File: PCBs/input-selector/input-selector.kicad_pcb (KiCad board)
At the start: 2 copper layers, 90.2 x 52.1 mm, 47 parts, among them J1 Conn_01x06_Male, K1 IM40, K2 IM40, K3 IM40, K4 IM40, K5 IM40, K6 IM40, U1 ULN2003, U2 MCP23S17_SO, U3 ULN2003

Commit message: small input selector update
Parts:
- C1: moved to B.Cu
- moved C1 8.39 mm to (127.8, 106.7)
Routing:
- net VDD: track 173.7 -> 172.4 mm
- net GND: vias 0 -> 3
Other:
- net class power: trace_width 0.8 -> 0.381
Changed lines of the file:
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@@
     (thickness 1.6)
     (drawings 25)
-    (tracks 328)
+    (tracks 333)
     (zones 0)
     (modules 47)
@@
   (net_class power ""
     (clearance 0.1524)
-    (trace_width 0.8)
+    (trace_width 0.381)
     (via_dia 0.8)
     (via_drill 0.3302)
@@
     )
   )
-  (module Capacitor_SMD:C_1206_3216Metric_Pad1.42x1.75mm_HandSolder (layer F.Cu)
-    (at 135.255 110.49 270)
+  (module Capacitor_SMD:C_1206_3216Metric_Pad1.42x1.75mm_HandSolder (layer B.Cu)
+    (at 127.762 106.7165 270)
     (descr "Capacitor SMD 1206 (3216 Metric), square (rectangular) end terminal, IPC_7351 nominal with elongated pad for handsoldering. (Body size source: http://www.tortai-tech.com/upload/download/2011102023233369053.pdf), generated with kicad-footprint-generator")
     (tags "capacitor handsolder")
     (attr smd)
-    (fp_text reference C1 (at 0 -1.82 270) (layer F.SilkS)
-      (effects (font (size 1 1) (thickness 0.15)))
+    (fp_text reference C1 (at 0 1.82 270) (layer B.SilkS)
+      (effects (font (size 1 1) (thickness 0.15)) (justify mirror))
     )
-    (fp_text value C (at 0 1.82 270) (layer F.Fab)
-      (effects (font (size 1 1) (thickness 0.15)))
+    (fp_text value C (at 0 -1.82 270) (layer B.Fab)
+      (effects (font (size 1 1) (thickness 0.15)) (justify mirror))
     )
-    (fp_line (start -1.6 0.8) (end -1.6 -0.8) (layer F.Fab) (width 0.1))
-    (fp_line (start -1.6 -0.8) (end 1.6 -0.8) (layer F.Fab) (width 0.1))
-    (fp_line (start 1.6 -0.8) (end 1.6 0.8) (layer F.Fab) (width 0.1))
-    (fp_line (start 1.6 0.8) (end -1.6 0.8) (layer F.Fab) (width 0.1))
-    (fp_line (start -0.602064 -0.91) (end 0.602064 -0.91) (layer F.SilkS) (width 0.12))
-    (fp_line (start -0.602064 0.91) (end 0.602064 0.91) (layer F.SilkS) (width 0.12))
-    (fp_line (start -2.45 1.12) (end -2.45 -1.12) (layer F.CrtYd) (width 0.05))
-    (fp_line (start -2.45 -1.12) (end 2.45 -1.12) (layer F.CrtYd) (width 0.05))
-    (fp_line (start 2.45 -1.12) (end 2.45 1.12) (layer F.CrtYd) (width 0.05))
-    (fp_line (start 2.45 1.12) (end -2.45 1.12) (layer F.CrtYd) (width 0.05))
-    (fp_text user %R (at 0 0 270) (layer F.Fab)
-      (effects (font (size 0.8 0.8) (thickness 0.12)))
+    (fp_line (start -1.6 -0.8) (end -1.6 0.8) (layer B.Fab) (width 0.1))
+    (fp_line (start -1.6 0.8) (end 1.6 0.8) (layer B.Fab) (width 0.1))
+    (fp_line (start 1.6 0.8) (end 1.6 -0.8) (layer B.Fab) (width 0.1))
+    (fp_line (start 1.6 -0.8) (end -1.6 -0.8) (layer B.Fab) (width 0.1))
+    (fp_line (start -0.602064 0.91) (end 0.602064 0.91) (layer B.SilkS) (width 0.12))
+    (fp_line (start -0.602064 -0.91) (end 0.602064 -0.91) (layer B.SilkS) (width 0.12))
+    (fp_line (start -2.45 -1.12) (end -2.45 1.12) (layer B.CrtYd) (width 0.05))
+    (fp_line (start -2.45 1.12) (end 2.45 1.12) (layer B.CrtYd) (width 0.05))
+    (fp_line (start 2.45 1.12) (end 2.45 -1.12) (layer B.CrtYd) (width 0.05))
+    (fp_line (start 2.45 -1.12) (end -2.45 -1.12) (layer B.CrtYd) (width 0.05))
+    (fp_text user %R (at 0 0 270) (layer B.Fab)
+      (effects (font (size 0.8 0.8) (thickness 0.12)) (justify mirror))
     )
-    (pad 1 smd roundrect (at -1.4875 0 270) (size 1.425 1.75) (layers F.Cu F.Paste F.Mask) (roundrect_rratio 0.175439)
+    (pad 1 smd roundrect (at -1.4875 0 270) (size 1.425 1.75) (layers B.Cu B.Paste B.Mask) (roundrect_rratio 0.175439)
       (net 65 VDD))
-    (pad 2 smd roundrect (at 1.4875 0 270) (size 1.425 1.75) (layers F.Cu F.Paste F.Mask) (roundrect_rratio 0.175439)
+    (pad 2 smd roundrect (at 1.4875 0 270) (size 1.425 1.75) (layers B.Cu B.Paste B.Mask) (roundrect_rratio 0.175439)
       (net 67 GND))
     (model ${KISYS3DMOD}/Capacitor_SMD.3dshapes/C_1206_3216Metric.wrl
@@
   (segment (start 167.639808 83.5025) (end 168.275 82.867308) (width 0.6) (layer B.Cu) (net 49))
   (segment (start 166.37 83.5025) (end 167.639808 83.5025) (width 0.6) (layer B.Cu) (net 49))
-  (segment (start 146.05 95.737) (end 146.537 95.25) (width 0.508) (layer F.Cu) (net 50))
+  (segment (start 160.401 94.869) (end 166.37 88.9) (width 0.508) (layer F.Cu) (net 50))
+  (segment (start 146.939 94.869) (end 160.401 94.869) (width 0.508) (layer F.Cu) (net 50))
+  (segment (start 146.05 95.737) (end 146.939 94.869) (width 0.508) (layer F.Cu) (net 50))
   (segment (start 146.05 96.995) (end 146.05 95.737) (width 0.508) (layer F.Cu) (net 50))
-  (segment (start 160.02 95.25) (end 166.37 88.9) (width 0.508) (layer F.Cu) (net 50))
-  (segment (start 146.537 95.25) (end 160.02 95.25) (width 0.508) (layer F.Cu) (net 50))
   (segment (start 101.6 76.13) (end 101.6 81.28) (width 0.6) (layer F.Cu) (net 52))
   (segment (start 101.6 74.93) (end 101.6 76.13) (width 0.6) (layer F.Cu) (net 52))
@@
   (segment (start 166.1525 94.1975) (end 168.91 91.44) (width 0.8) (layer B.Cu) (net 65))
   (segment (start 168.91 91.44) (end 171.45 88.9) (width 0.8) (layer B.Cu) (net 65))
-  (segment (start 147.32 98.2075) (end 147.32 94.615) (width 0.8) (layer B.Cu) (net 65))
   (segment (start 117.475 98.2075) (end 117.475 94.615) (width 0.8) (layer B.Cu) (net 65))
   (segment (start 115.57 94.1975) (end 117.0575 94.1975) (width 0.8) (layer B.Cu) (net 65))
@@
   (segment (start 165.735 94.1975) (end 166.1525 94.1975) (width 0.8) (layer B.Cu) (net 65))
   (segment (start 162.9775 94.1975) (end 162.56 94.615) (width 0.8) (layer B.Cu) (net 65))
-  (segment (start 134.8375 108.585) (end 135.255 109.0025) (width 0.381) (layer F.Cu) (net 65))
-  (segment (start 132.335 108.585) (end 134.8375 108.585) (width 0.381) (layer F.Cu) (net 65))
-  (segment (start 122.935 106.045) (end 125.095 106.045) (width 0.381) (layer F.Cu) (net 65))
-  (segment (start 127.635 108.585) (end 132.335 108.585) (width 0.381) (layer F.Cu) (net 65))
-  (segment (start 125.095 106.045) (end 127.635 108.585) (width 0.381) (layer F.Cu) (net 65))
-  (via (at 147.32 99.187) (size 0.8) (drill 0.4) (layers F.Cu B.Cu) (net 65))
-  (segment (start 147.32 96.995) (end 147.32 99.187) (width 0.381) (layer F.Cu) (net 65))
-  (segment (start 147.32 99.187) (end 147.32 98.2075) (width 0.381) (layer B.Cu) (net 65))
   (via (at 117.475 96.012) (size 0.8) (drill 0.4) (layers F.Cu B.Cu) (net 65))
   (segment (start 117.475 96.995) (end 117.475 96.012) (width 0.381) (layer F.Cu) (net 65))
-  (via (at 125.095 106.045) (size 0.8) (drill 0.4) (layers F.Cu B.Cu) (net 65))
   (segment (start 125.095 94.8325) (end 124.46 94.1975) (width 0.381) (layer B.Cu) (net 65))
-  (segment (start 125.095 106.045) (end 125.095 94.8325) (width 0.381) (layer B.Cu) (net 65))
   (segment (start 96.52 105.41) (end 98.425 105.41) (width 0.8) (layer F.Cu) (net 65))
   (segment (start 104.267 111.252) (end 105.505 111.252) (width 0.8) (layer F.Cu) (net 65))
@@
   (segment (start 105.1925 111.5645) (end 105.505 111.252) (width 0.8) (layer F.Cu) (net 65))
   (segment (start 105.1925 119.38) (end 105.1925 111.5645) (width 0.8) (layer F.Cu) (net 65))
+  (segment (start 147.32 96.012) (end 147.32 94.615) (width 0.8) (layer B.Cu) (net 65))
+  (via (at 147.32 96.012) (size 0.8) (drill 0.3302) (layers F.Cu B.Cu) (net 65))
+  (segment (start 127.762 94.7055) (end 128.27 94.1975) (width 0.8) (layer B.Cu) (net 65))
+  (segment (start 127.762 105.229) (end 127.762 94.7055) (width 0.8) (layer B.Cu) (net 65))
+  (segment (start 147.32 98.2075) (end 147.32 96.012) (width 0.8) (layer B.Cu) (net 65))
+  (segment (start 147.32 96.995) (end 147.32 96.012) (width 0.381) (layer F.Cu) (net 65))
+  (segment (start 127.762 105.229) (end 127.562 105.229) (width 0.381) (layer B.Cu) (net 65))
+  (segment (start 127.562 105.229) (end 126.746 106.045) (width 0.381) (layer B.Cu) (net 65))
+  (segment (start 126.746 106.045) (end 124.206 106.045) (width 0.381) (layer B.Cu) (net 65))
+  (via (at 117.475 103.378) (size 0.8) (drill 0.3302) (layers F.Cu B.Cu) (net 67))
+  (via (at 147.32 103.378) (size 0.8) (drill 0.3302) (layers F.Cu B.Cu) (net 67))
+  (via (at 124.206 106.045) (size 0.8) (drill 0.3302) (layers F.Cu B.Cu) (net 65))
+  (segment (start 129.032 108.585) (end 132.335 108.585) (width 0.381) (layer F.Cu) (net 65))
+  (segment (start 126.492 106.045) (end 129.032 108.585) (width 0.381) (layer F.Cu) (net 65))
+  (segment (start 122.935 106.045) (end 126.492 106.045) (width 0.381) (layer F.Cu) (net 65))
+  (via (at 124.206 107.315) (size 0.8) (drill 0.3302) (layers F.Cu B.Cu) (net 67))
   (segment (start 157.48 114.935) (end 157.48 116.205) (width 0.381) (layer F.Cu) (net 68))
   (segment (start 125.095 109.855) (end 129.54 114.3) (width 0.381) (layer F.Cu) (net 68))

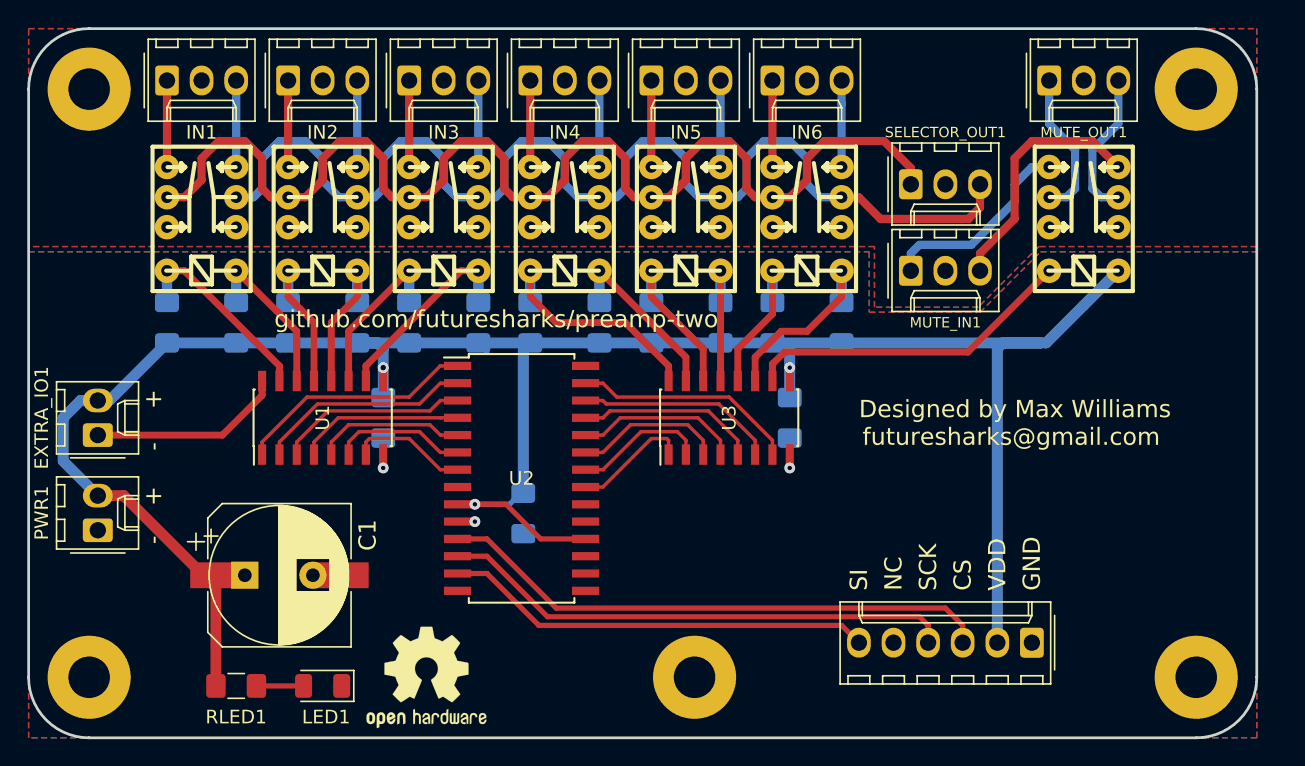
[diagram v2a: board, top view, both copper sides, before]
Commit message: Fixing input selector panasonic relay footprint
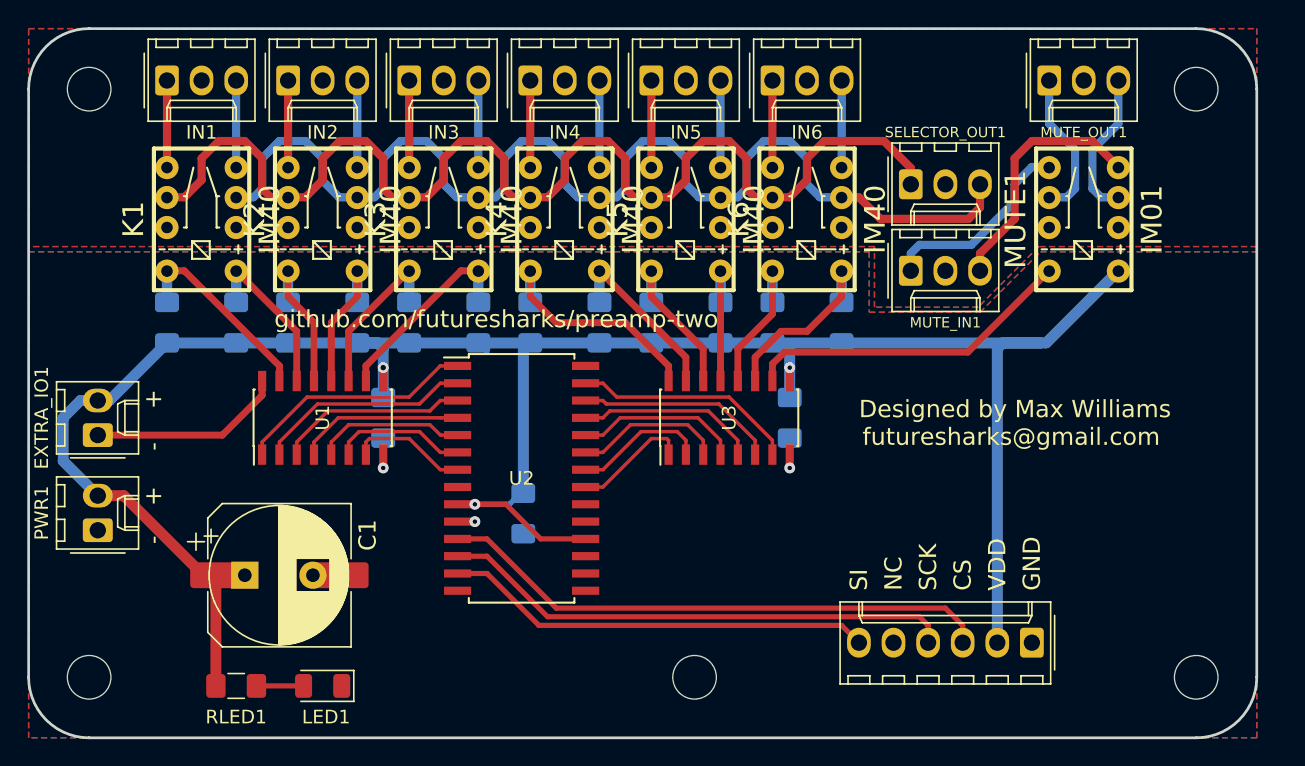
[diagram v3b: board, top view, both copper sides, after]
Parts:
- removed REF**: OSHW-Logo2_9.8x8mm_SilkScreen, Symbol:OSHW-Logo2_9.8x8mm_SilkScreen
- K1, K2, K3, K4, K5, K6, MUTE1: footprint w_relay:relay_gq-pth -> panasonic-relay:gq-th
- moved K1 0.63 mm to (104.1, 85.7)
- moved K2 0.63 mm to (113.0, 85.7)
- moved K3 0.63 mm to (121.9, 85.7)
- moved K4 0.63 mm to (130.8, 85.7)
- moved K5 0.63 mm to (139.7, 85.7)
- moved K6 0.63 mm to (148.6, 85.7)
- moved MUTE1 0.63 mm to (168.9, 85.7)

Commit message: Switching relay type to Omron G6J relays
Since I can't find a source for the others
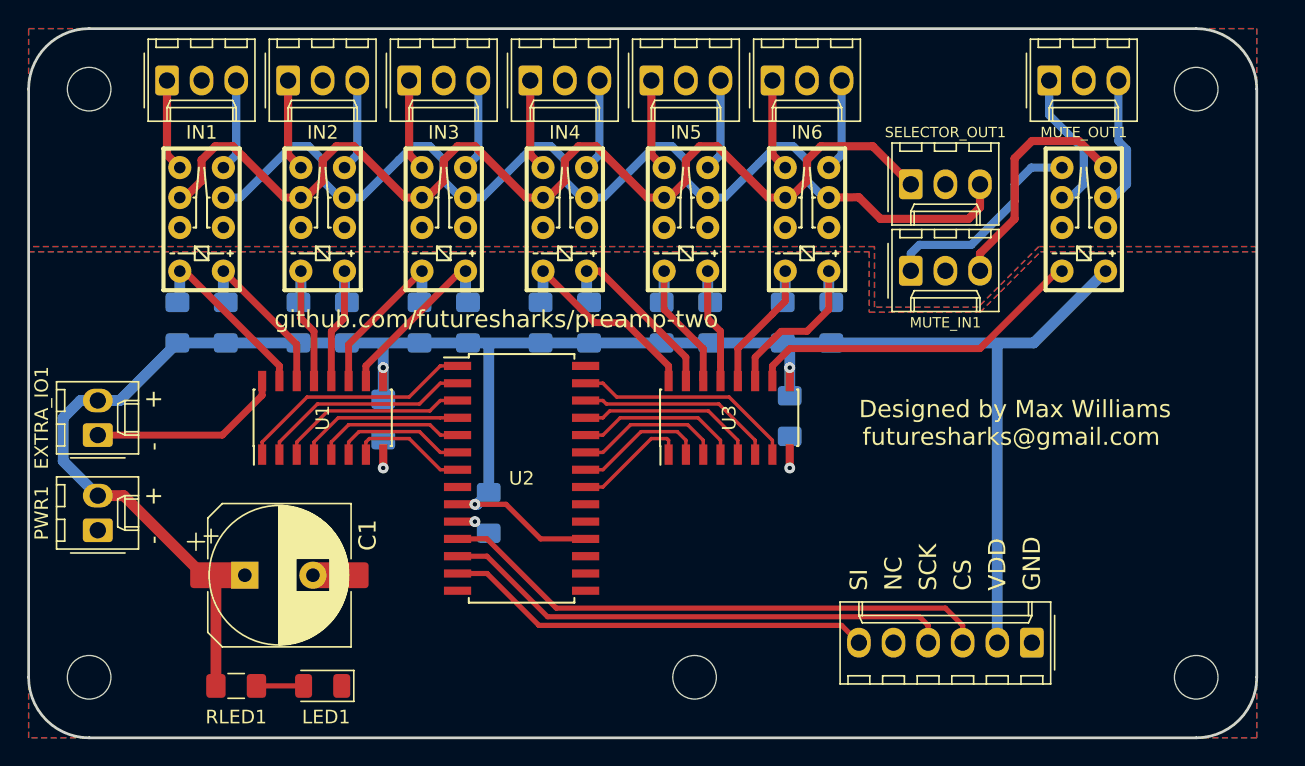
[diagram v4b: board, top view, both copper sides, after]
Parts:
- K1, K2, K3, K4, K5, K6, MUTE1: footprint panasonic-relay:gq-th -> omron-relay:g6j-2p-y
- moved C1 2.54 mm to (125.2, 106.7)
- moved R1 0.76 mm to (123.7, 92.7)
- moved R10 0.76 mm to (137.9, 92.7)
- moved R11 0.76 mm to (132.6, 92.7)
- moved R12 0.76 mm to (129.0, 92.7)
- moved R2 0.76 mm to (120.1, 92.7)
- moved R4 0.76 mm to (111.3, 92.7)
- moved R5 0.76 mm to (105.9, 92.7)
- moved R6 0.76 mm to (102.4, 92.7)
- moved R7 0.76 mm to (150.4, 92.7)
- moved R8 0.76 mm to (146.8, 92.7)
- moved R9 0.76 mm to (141.5, 92.7)
- moved R3 0.76 mm to (114.8, 92.7)
- moved C3 0.13 mm to (117.5, 99.8)
- moved C2 0.13 mm to (147.3, 99.6)
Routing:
- net Net-(K1-Pad6): track 87.5 -> 77.4 mm
- net VDD: track 172.4 -> 162.3 mm
- net Net-(K1-Pad3): track 86.4 -> 78.3 mm
- net Net-(K4-Pad8): track 17.6 -> 15.6 mm
- net Net-(MUTE1-Pad8): track 24.4 -> 25.6 mm
- net Net-(MUTE1-Pad3): track 10.9 -> 9.86 mm
- net Net-(K4-Pad1): track 13.5 -> 14.5 mm
- net Net-(MUTE1-Pad5): track 15.4 -> 16.4 mm
- net Net-(MUTE1-Pad4): track 18.9 -> 18.0 mm
- net Net-(K1-Pad8): track 14.6 -> 13.7 mm
- net Net-(K3-Pad1): track 14.6 -> 13.7 mm
- net Net-(K5-Pad1): track 10.4 -> 11.0 mm
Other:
- net class Default: trace_width 0.381 -> 0.8
- net class power: trace_width 0.381 -> 0.8
